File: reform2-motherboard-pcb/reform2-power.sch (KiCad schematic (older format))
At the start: 193 parts, among them J1 Jack-DC, J13 BATCON1, J2 BATCON2, J22 LPC_IO, J23 KDBSYSCTL, J8 USB_B_Micro, Q1 Si7850DP, Q10 PMV50EPEAR, Q11 PMV50EPEAR, Q12 PMV50EPEAR, Q15 Si7850DP, Q17 Si7850DP, Q18 Si7461DP, Q2 Si7850DP, Q3 Si7461DP, Q5 PMV50EPEAR, Q6 PMV50EPEAR, Q7 PMV50EPEAR, Q8 PMV50EPEAR, Q9 PMV50EPEAR, SW1 SW_LPCPROG, SW2 SW_LPCRST, U12 LM2677SX-3.3, U13 TLV62568DBV, U14 LM2841X, U17 TLV1117-18, U18 LPC11U24FBD48-301, U19 TLV62568DBV, U2 LTC4020EUHFPBF, U4 LTC6803-4, U5 PCF8523T, U6 INA260, U7 LM2677SX-5, Y2 12MHz, Y4 32.768 kHz

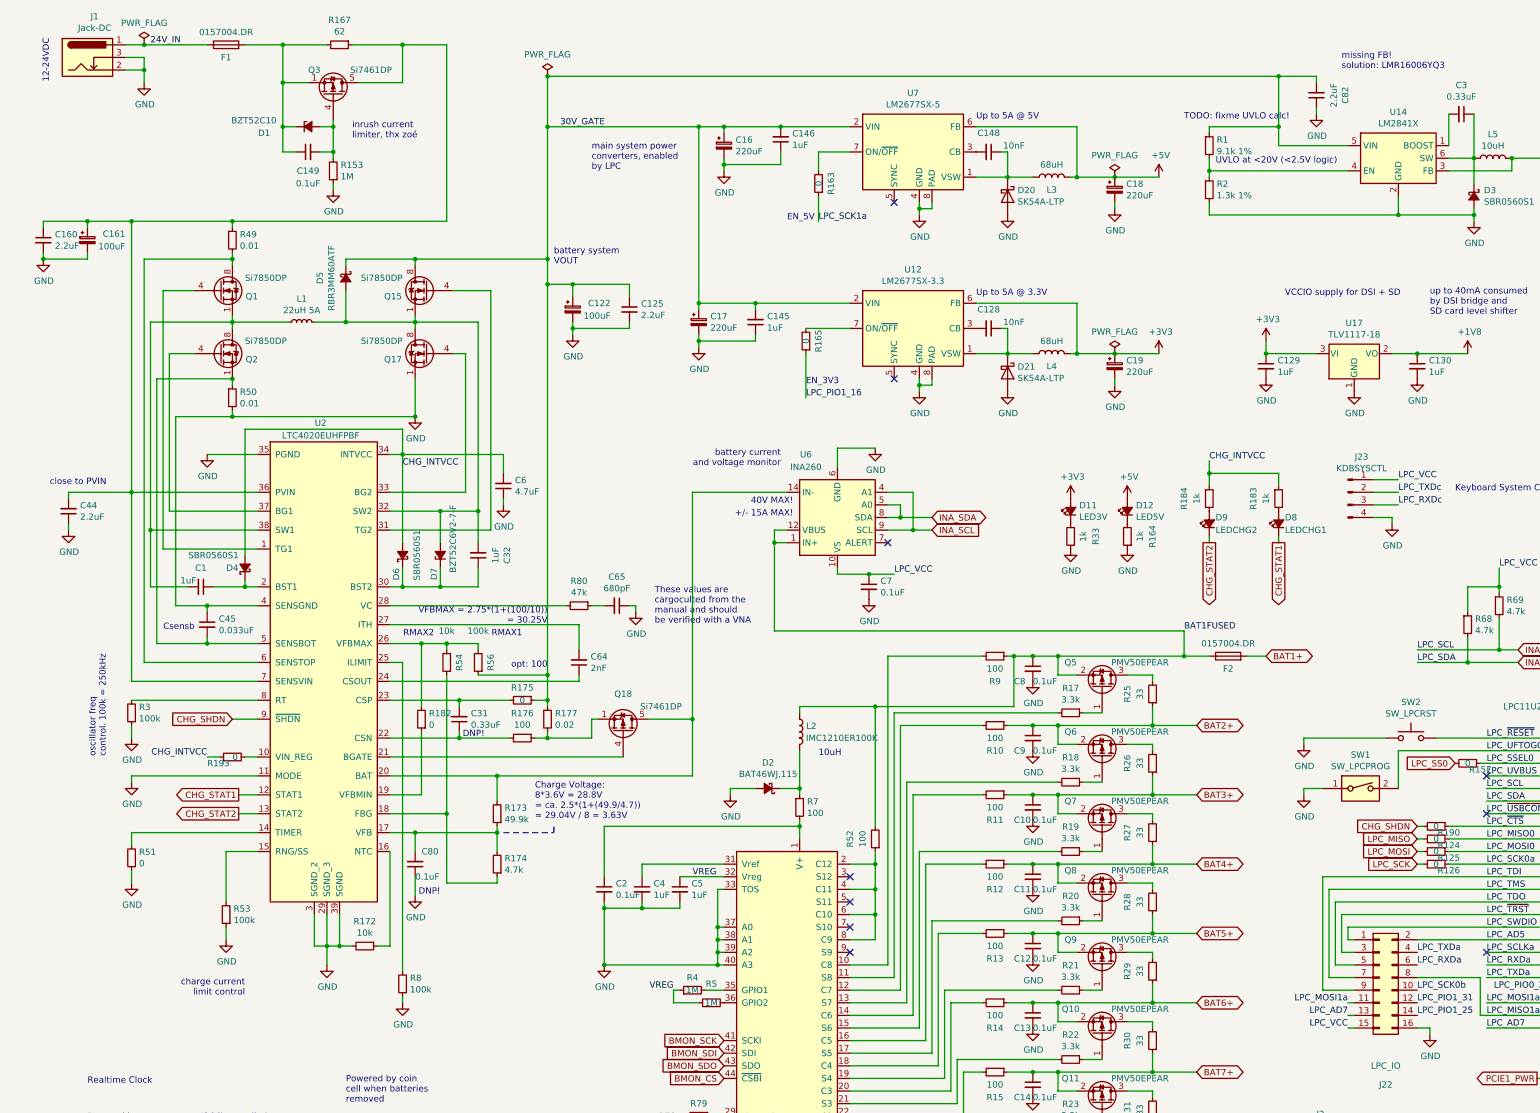
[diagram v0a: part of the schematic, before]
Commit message: WIP license clarification, motherboard now CERN-OHL-S 2.0
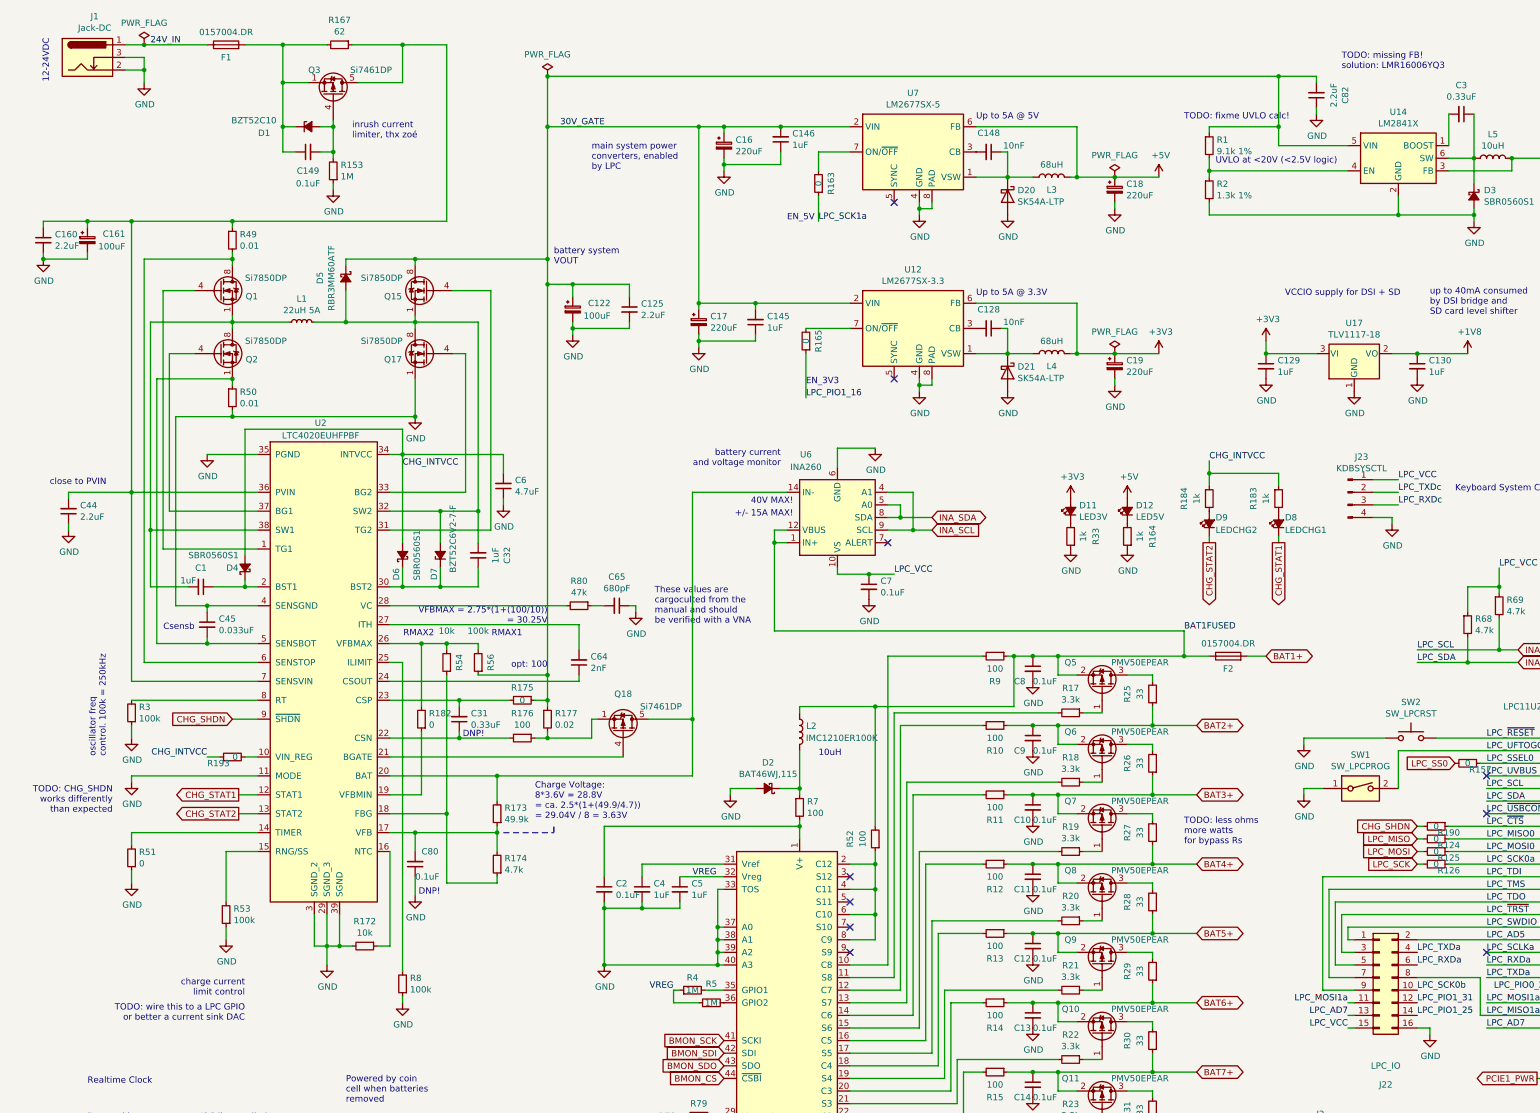
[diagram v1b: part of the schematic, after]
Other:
- note added: "TODO: CHG_SHDN\nworks differently\nthan expected"
- note added: "TODO: less ohms\nmore watts\nfor bypass Rs"
- note added: "TODO: missing FB!\nsolution: LMR16006YQ3"
- note added: "TODO: wire this to a LPC GPIO\nor better a current sink DAC"
- note removed: "missing FB!\nsolution: LMR16006YQ3"
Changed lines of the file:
@@
 EESchema Schematic File Version 4
-LIBS:reform2-motherboard-cache
-EELAYER 29 0
+EELAYER 30 0
 EELAYER END
 $Descr A3 16535 11693
@@
 Sheet 9 9
 Title "MNT Reform 2 Power System"
-Date "2020-02-10"
-Rev "2.0D-3"
+Date "2020-04-11"
+Rev "2.0D-4"
 Comp "MNT Research GmbH"
 Comment1 "https://mntre.com"
 Comment2 "Engineer: Lukas F. Hartmann"
-Comment3 "License: GPL v3+"
+Comment3 "License: CERN-OHL-S 2.0"
 Comment4 ""
 $EndDescr
@@
 Text Notes 8000 1350 0    50   ~ 0
 Up to 5A @ 5V
-$Bitmap
-Pos 15550 10300
-Scale 1.000000
-Data
-89 50 4E 47 0D 0A 1A 0A 00 00 00 0D 49 48 44 52 00 00 01 2C 00 00 00 70 08 06 00 00 00 A4 46 4D
-4D 00 00 00 04 73 42 49 54 08 08 08 08 7C 08 64 88 00 00 06 2D 49 44 41 54 78 9C ED DD BB 8B 1D
-65 1C 87 F1 67 77 45 B1 08 82 26 F1 D2 6A 5A FF 00 0B B5 16 4C 36 12 5D 2F 9D 69 BC 04 0D 5E 62
-A3 A4 B1 D0 CE 4B C4 24 42 2A 05 03 21 85 FA 07 68 B4 8A 60 67 21 12 6D 04 0D 1A 90 04 4C 97 B5
-98 19 CE 64 F7 9C 39 B7 77 DE DF 7B F6 3C 1F 38 EC 16 CB EC 97 2D 1E 66 66 77 CF 80 24 49 92 24
-49 92 24 49 92 24 49 92 24 49 92 24 49 92 24 49 92 24 49 92 24 49 92 24 49 52 42 8F 00 7B A2 47
-B4 1C 8A 1E D0 F2 10 70 5F F4 08 49 03 C7 81 B3 94 13 AD 3F 80 67 A2 47 D4 8E 02 DF 60 B4 A4 62
-1C 07 36 29 27 5A D7 81 7F 28 23 5A 47 A9 7E 36 5F 63 B4 A4 22 34 C1 2A 25 5A D7 EB 2D 25 44 AB
-09 96 D1 92 0A D1 0E 56 09 D1 6A 82 55 42 B4 DA C1 32 5A 52 01 B6 06 AB 89 D6 EE A0 3D ED 60 45
-47 6B 6B B0 8C 96 14 6C 58 B0 22 A3 B5 35 58 91 D1 1A 16 2C A3 25 05 1A 15 AC A8 68 0D 0B 56 54
-B4 46 05 AB 89 D6 BD 99 F7 48 4B AF 2B 58 11 D1 1A 15 AC 88 68 75 05 6B 13 F8 0A A3 25 65 35 2E
-58 B9 A3 D5 15 AC 4D E0 6F F2 45 6B 5C B0 8C 96 94 D9 24 C1 DA 04 BE 24 4F B4 C6 05 2B 67 B4 26
-09 96 D1 92 32 9A 34 58 B9 A2 35 49 B0 9A 68 3D DD F3 96 49 83 65 B4 34 97 5B A2 07 EC 50 1B F5
-C7 23 54 F7 93 22 ED 06 3E 66 70 C9 1A ED 71 AA 2D 2F 00 7F F6 F4 3D 1E 05 6E ED E9 D8 7D B8 54
-BF 34 86 C1 EA 4F 69 D1 3A 51 7F 5E 42 B4 F6 D7 1F FB 8A D6 67 C4 FF 27 C2 34 DE AB 5F 1A C3 60
-F5 CB 68 8D D6 67 B4 76 01 77 24 3E 66 9F 6E 8B 1E B0 28 56 A3 07 2C 81 0D AA 50 44 FD 45 7C 5B
-13 AD 8D 71 5F 98 C9 7E E0 24 DE D3 D2 84 0C 56 1E 1B 54 F7 91 EE 8A 1E C2 E0 9E 96 D1 D2 C2 31
-58 F9 94 14 AD 3D 18 2D 2D 20 83 95 CF 0A D5 9F 17 18 AD E1 8C 96 C6 32 58 79 95 1A AD A7 A2 87
-D4 8C 96 3A 19 AC FC 4A 8C D6 09 8C 96 16 80 C1 8A 61 B4 BA ED 07 3E 05 EE 89 1E A2 B2 18 AC 38
-46 AB DB 01 E0 14 46 4B 2D 06 2B 96 D1 EA D6 5C 1E 1A 2D 01 06 AB 04 4D B4 3E C2 68 0D 73 80 EA
-F2 F0 EE E8 21 8A 67 B0 CA B0 42 F5 36 30 46 6B B8 75 AA 33 2D A3 B5 E4 0C 56 39 8C 56 37 A3 25
-83 55 98 52 A3 F5 64 F4 90 9A D1 5A 72 06 AB 3C A5 46 EB 50 F4 90 DA 3A DE D3 5A 5A 06 AB 4C A5
-45 6B 2F F0 09 E5 44 EB 20 46 6B 29 F9 7E 58 E5 6A A2 05 F0 0A 70 25 70 0B 0C A2 05 70 2E 72 48
-ED 60 FD F1 45 E0 72 0F C7 FF 17 F8 BC 87 E3 0E 73 31 D3 F7 D1 12 99 E6 3D DD 53 BE 6E 00 5F 00
-77 6E D9 33 E9 7B BA A7 7E 5D 66 FB 99 D6 34 EF E9 9E FA 75 9E ED 67 5A 7F 25 38 EE 2F A8 38 5E
-12 96 AF 7D 79 B8 35 5A 11 BC 3C 54 18 83 B5 18 56 80 67 81 0F 31 5A C3 18 AD 25 E1 3D AC C5 B1
-02 3C 57 7F FE 6A E4 90 5A FB 9E 56 09 DA F7 B4 B4 43 19 AC C5 D2 8E 56 09 67 C7 4D B4 7E 8C 1E
-52 6B A2 E5 43 1D 76 28 83 B5 78 DA D1 2A C1 5E E0 B1 E8 11 2D 07 A9 6E 9A 6B 07 32 58 8B 69 25
-7A C0 16 EE 51 16 25 5C 56 48 D2 44 0C 96 A4 85 61 B0 24 2D 0C 83 25 69 61 18 AC FC 4A FA 0D 56
-49 5B A0 BC 3D 2A 8C C1 CA EF 2C F0 5F F4 88 DA EF C0 B7 D1 23 5A CE 01 57 A3 47 A8 5C 06 2B BF
-33 C0 DB 94 11 AD 2B C0 61 CA 89 D6 59 E0 4D 8C 96 46 30 58 F9 DD A0 FA 9F C0 52 A2 F5 1B E5 44
-6B 13 38 8D D1 D2 08 06 2B 86 D1 EA 66 B4 34 94 C1 8A 63 B4 BA 19 2D 6D 63 B0 62 19 AD 6E 46 4B
-37 31 58 F1 8C 56 B7 D3 C0 31 8C 96 30 58 A5 30 5A DD 8C 96 00 83 55 92 52 A3 F5 5D F4 10 06 BF
-3D 3C 06 5C 0B DE A2 40 06 AB 2C 4D B4 DE A1 9C 68 3D 8F D1 52 21 0C 56 79 6E 00 1F 60 B4 86 D9
-04 4E 61 B4 96 96 C1 2A 93 D1 1A AD 89 D6 5B 18 AD A5 63 B0 CA 55 62 B4 0E 03 17 A2 87 50 45 EB
-24 46 6B E9 18 AC B2 95 16 AD 4B 54 67 5A 46 4B 21 7C 4F F7 C9 9D 07 7E 4D 70 9C 9F A7 FC FA 26
-5A 00 EF 02 B7 27 D8 30 8F 26 5A 67 80 87 83 B7 34 D1 02 78 1F D8 15 B8 45 52 CB 2A F0 1A D5 99
-56 AA C7 BC 5F 9C 63 CF FD 54 F7 B4 52 3E 76 FE 89 19 B7 AC 50 3D 8F F0 6A C2 2D 3E AA 5E 9A D3
-2A F0 3A E9 A2 35 4F B0 20 7D B4 66 0D 16 A4 8F 96 C1 92 12 58 05 DE 20 4D B4 E6 0D 16 C0 03 A4
-8B D6 3C C1 82 B4 D1 32 58 52 22 A9 A2 95 22 58 90 2E 5A F3 06 0B D2 45 CB 60 49 09 A5 88 56 AA
-60 41 9A 68 A5 08 16 A4 89 96 C1 92 12 9B 37 5A 29 83 05 55 B4 2E CC B8 25 65 B0 60 FE 68 19 2C
-A9 07 F3 44 2B 75 B0 60 BE 68 A5 0C 16 0C A2 75 6D 86 2D 06 4B EA C9 AC D1 EA 23 58 30 7B B4 52
-07 0B 66 8F 96 C1 92 7A 34 4B B4 FA 0A 16 CC 16 AD 3E 82 05 55 B4 5E 62 BA 68 19 2C A9 67 6B 4C
-17 AD 3E 83 05 D3 47 AB AF 60 C1 F4 D1 32 58 52 06 D3 44 AB EF 60 C1 74 D1 EA 33 58 50 45 EB 65
-26 8B 96 C1 92 32 99 34 5A 39 82 05 93 47 AB EF 60 C1 E4 D1 32 58 52 46 6B 54 4F 9C E9 8A 56 AE
-60 C1 64 D1 CA 11 2C 98 2C 5A 06 4B CA 6C 5C B4 72 06 0B AA 68 7D 3F 62 4B CE 60 C1 F8 68 19 2C
-29 40 57 B4 72 07 0B 60 1F A3 A3 95 33 58 D0 1D 2D 83 25 05 19 15 AD 88 60 C1 E8 68 E5 0E 16 8C
-8E 96 C1 92 02 0D 8B 56 54 B0 A0 8A D6 0F C4 07 0B 86 47 CB 60 49 C1 D6 A8 9E 38 73 9D F8 60 C1
-F6 68 45 05 0B AA 68 1D 61 10 2D 83 25 15 A0 1D AD E8 60 C1 CD D1 8A 0C 16 DC 1C 2D 83 25 15 A2
-89 56 09 0F 93 80 41 B4 A2 83 05 83 68 FD 14 3D 44 D2 C0 1A B0 1E 3D A2 65 1F F0 60 F4 88 DA 0A
-65 C4 53 92 24 49 92 24 49 92 24 49 92 24 49 92 24 49 92 24 49 92 24 49 92 24 49 92 24 49 52 41
-FE 07 39 BD 85 89 55 AA C4 B1 00 00 00 00 49 45 4E 44 AE 42 60 82
-EndData
-$EndBitmap
 $Comp
 L Device:C_Small C128
@@
 LPC_MOSI1a
 Text Notes 10900 950  0    50   ~ 0
-missing FB!\nsolution: LMR16006YQ3
+TODO: missing FB!\nsolution: LMR16006YQ3
+Text Notes 2200 8500 2    50   ~ 0
+TODO: wire this to a LPC GPIO\nor better a current sink DAC
+Text Notes 9650 7100 0    50   ~ 0
+TODO: less ohms\nmore watts\nfor bypass Rs
+Text Notes 1150 6850 2    50   ~ 0
+TODO: CHG_SHDN\nworks differently\nthan expected
 $EndSCHEMATC

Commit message: reform2-motherboard: version D-4 finished; fixes critical D-3 bugs; adds PCIe refclk termination, speaker output filter stage, pcie0 3v3 load switch, imx reset line to lpc, charge current control line to lpc
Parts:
- added R162: 10k, Resistor_SMD:R_0603_1608Metric, symbol Device:R_Small
- added R194: 0, Resistor_SMD:R_0603_1608Metric, symbol Device:R_Small
- added R195: 1.5k, Resistor_SMD:R_0603_1608Metric, symbol Device:R_Small
- C80, R127, R190: DNP (none) -> y
- R175: value 0 -> 100; Manufacturer_No CRCW06030000Z0EAC -> CRCW0603100RFKEAC
- R25, R26, R27, R28, R29, R30, R31, R32: value 33 -> 4.7; footprint Resistor_SMD:R_0603_1608Metric -> Resistor_SMD:R_2512_6332Metric; Manufacturer Vishay Dale -> TE Connectivity; Manufacturer_No CRCW060333R0FKEAC -> 35224R7JT
- R53: value 100k -> 330; Manufacturer Vishay Dale -> Yageo; Manufacturer_No CRCW0603100KJNEAC -> RC0603FR-07330RL
- U14: value LM2841X -> LMR16006YQ3; Manufacturer_No LM2841XMK-ADJL/NOPB -> LMR16006YQ3
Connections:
- net GND: no longer R53.1
- net LPC_SCLKa: now also J22.14 (Pin_14)
- net LPC_SCLKc: now also R194.2
- net LPC_UVBUS: now also R195.2
- net LPC_VCC: now also R195.1
- net at R193.2, U2.10 (VIN_REG): now also R162.2
- net CHG_SHDN: no longer names the net of U2.9 (~SHDN)
- net CHG_SHDN: now also R162.1; no longer R190.2
- net LPC_PIO1_25 renamed CHG_RNG
- net CHG_RNG: now also R53.1; no longer J22.14 (Pin_14)
- new net IMX_RESETn: R194.1
- no-connect marks 12 -> 10
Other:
- note added: "Battery system\nVOUT"
- note added: "FIXME: confirm\ntemperature stress\nof balancing Rs"
- note added: "Main system power\nconverters, enabled\nby LPC"
- note added: "TODO: check UVLO calc!"
- note added: "charge current\nlimit control\n(toggles no charge\n/no limit)"
- note added: "inrush current\nlimiter, thanks zoé"
- note added: "up to 1A (peak)\n375mA normal \nfrom mPCIe"
- note removed: "Battery cable: Molex 45130-1003 (30cm, 10pos, 2rows)"
- note removed: "DNP!"
- note removed: "TODO: CHG_SHDN\nworks differently\nthan expected"
- note removed: "TODO: connect chgstat 1+2 to LPC?\n"
- note removed: "TODO: fixme UVLO calc!"
- note removed: "TODO: less ohms\nmore watts\nfor bypass Rs"
- note removed: "TODO: missing FB!\nsolution: LMR16006YQ3"
- note removed: "TODO: wire this to a LPC GPIO\nor better a current sink DAC"
- note removed: "battery system\nVOUT"
- note removed: "charge current\nlimit control"
- note removed: "inrush current\nlimiter, thx zoé"
- note removed: "main system power\nconverters, enabled\nby LPC"
- note removed: "opt: 100"
- note removed: "up to 1A (peak)\n2x375mA normal \nfrom 2x mPCIe"
- moved on the sheet: C31, C48, C51, R193, R53, R73, R74, R75, R76, R8, Y2
